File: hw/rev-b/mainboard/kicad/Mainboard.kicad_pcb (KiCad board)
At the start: 2 copper layers, 262.5 x 95.2 mm, 304 parts, among them J1 IEEE_EDGE, J10 5V PWR, J11 9V POWER, J12 VIDEO_OR_5V, J13 9V POWER JACK, J14 USER_HEADER, J15 CASS_A_HEADER, J16 CASS_B_HEADER, J17 PMOD1, J18 PMOD2, J19 KEYBOARD_EX, J2 USER_EDGE, J20 IEEE_HEADER, J21 AUDIO, J22 PROG, J23 MENU, J24 NOT_HDMI_A, J25 MICRO_SD, J26 USB1.1_HOST_TYPE_C, J27 6V POWER, J28 5V POWER, J3 CASS_A_EDGE, J4 BUS_EXPANSION, J5 KEYBOARD, J6 CASS_B_EDGE, J7 VIDEO, J8 PET POWER, J9 FPGA_MCU, Q1 MMBT3904, Q2 AO3401A, Q3 AO3401A, Q4 SS8050, Q5 SS8050, Q6 SS8050, Q7 SS8550, SW1 TS-1088-AR02016, SW2 TS-1088-AR02016, SW3 CONFIG, SW4 TS-1088-AR02016, SW5 MENU_BTN, SW6 TS-1088-AR02016, U1 W65C02S, U10 T20Q144C3, U11 W65C21N, U12 W65C21N, U13 W65C22N, U14 SN74LS07, U15 SN74LS07, U16 SN74LS07, U17 74LS245, U18 74LS245, U19 74LS145, U2 IS62WV1288BLL-55QLI, U21 RP2040, U22 W25Q128JVS, U3 AMS1117-3.3, U4 TPS564247DRLR, U5 LM317AG-TN3-R, U6 TPS564247DRLR, U7 SN74LVC4245A, U8 SN74LVC4245A, U9 SN74LVC4245A, Y1 12 MHz

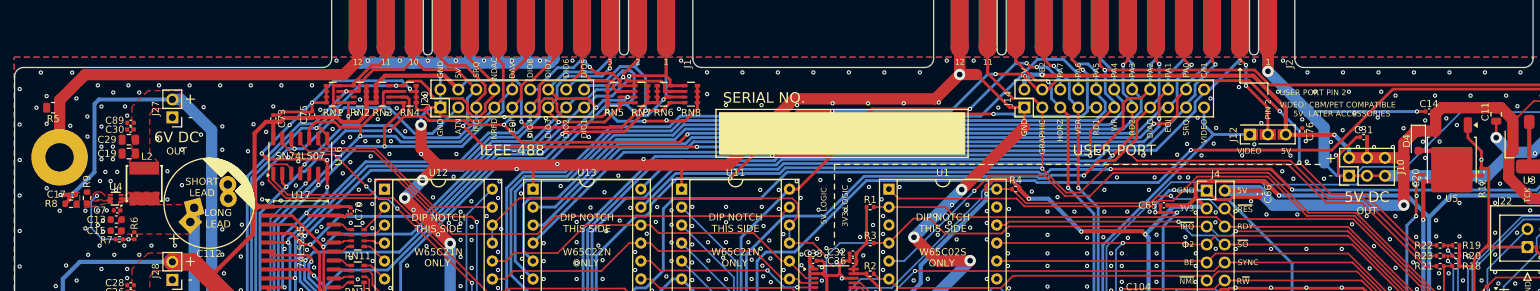
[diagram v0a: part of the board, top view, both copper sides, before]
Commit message: feat(hw): avoid 68R extended part
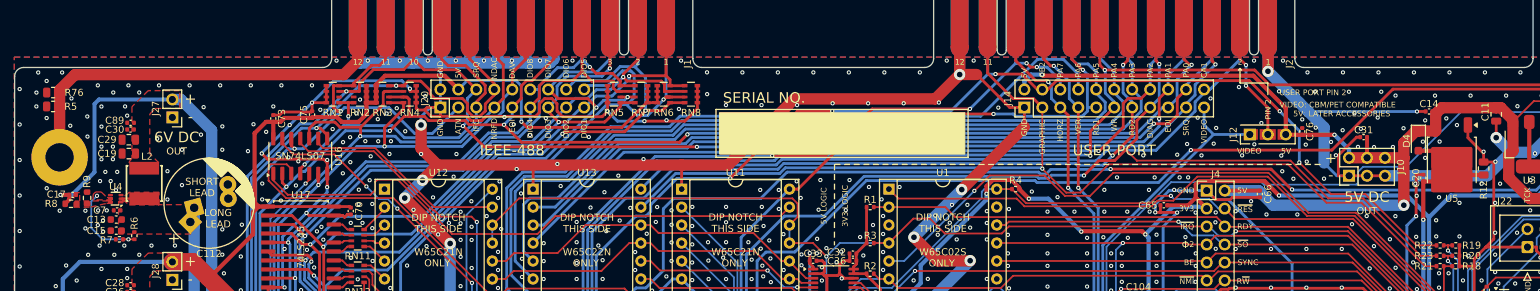
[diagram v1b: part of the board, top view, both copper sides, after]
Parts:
- added R76: 150, Resistor_SMD:R_0805_2012Metric, F.Cu at (96.5, 97.3)
- R12: footprint Resistor_SMD:R_0402_1005Metric -> Resistor_SMD:R_0805_2012Metric
- R5: value 68 -> 120
- moved R12 0.58 mm to (298.8, 108.1)
- moved R5 0.18 mm to (96.5, 99.3)
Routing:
- net CHASSIS_GND: track 54.3 -> 55.2 mm
- net GND: track 2240.0 -> 2240.9 mm, vias 1810 -> 1813
